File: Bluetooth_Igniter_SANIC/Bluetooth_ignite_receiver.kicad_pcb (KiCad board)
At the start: 2 copper layers, 62.3 x 30 mm, 68 parts, among them J1 Screw_Terminal_01x02, J2 Screw_Terminal_01x02, J3 Screw_Terminal_01x02, J4 Screw_Terminal_01x02, J5 USB_C_Receptacle_USB2.0, J6 Conn_01x02_Male, J7 Conn_01x02_Male, Q1 MMDT2222A, Q2 MMDT2222A, Q3 Q_NMOS_GSD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

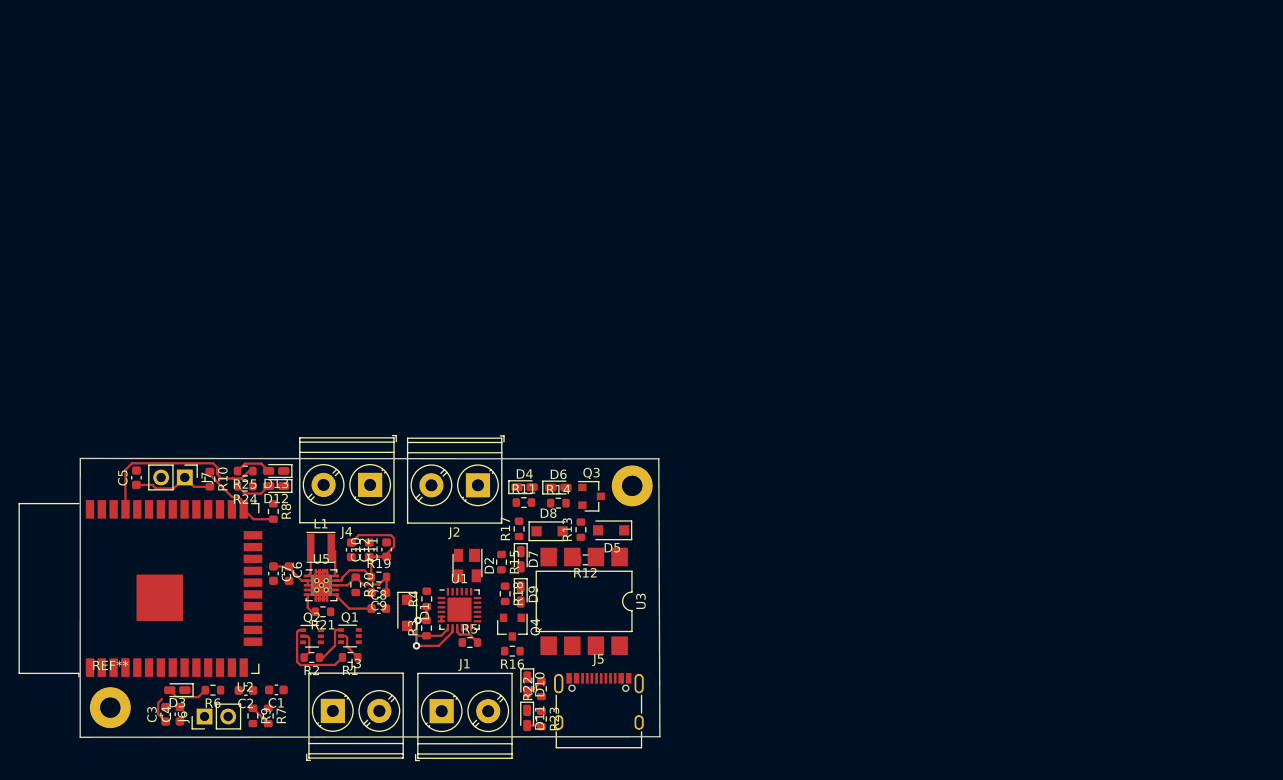
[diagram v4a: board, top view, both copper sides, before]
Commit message: need to fit pin headers in
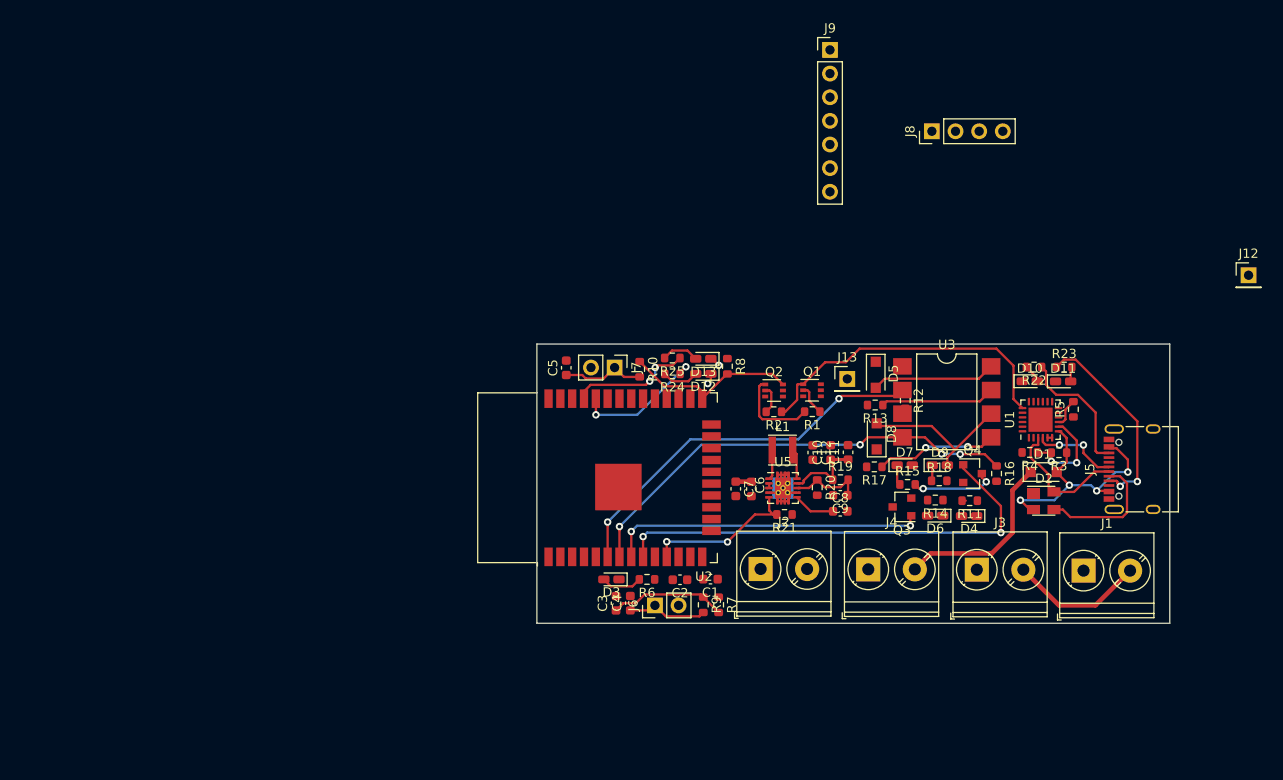
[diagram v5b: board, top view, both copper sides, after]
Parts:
- removed REF** (x2): MountingHole_2.2mm_M2_Pad, MountingHole:MountingHole_2.2mm_M2_Pad
- added J12: Conn_01x01_Male, Connector_PinHeader_2.54mm:PinHeader_1x01_P2.54mm_Vertical, F.Cu at (153.0, 67.9)
- added J13: Conn_01x01_Male, Connector_PinHeader_2.54mm:PinHeader_1x01_P2.54mm_Vertical, F.Cu at (109.9, 79.1)
- added J8: Conn_01x04_Male, Connector_PinHeader_2.54mm:PinHeader_1x04_P2.54mm_Vertical, F.Cu at (119.0, 52.5)
- added J9: Conn_01x07_Male, Connector_PinHeader_2.54mm:PinHeader_1x07_P2.54mm_Vertical, F.Cu at (108.1, 43.7)
- moved J3 70.8 mm to (123.9, 99.6)
- moved J1 70.6 mm to (135.3, 99.7)
- moved R3 70.5 mm to (132.7, 87.0), turned to 180 degrees
- moved D1 70.0 mm to (131.0, 89.1), turned to 0 degrees
- moved R5 69.5 mm to (134.2, 82.3), turned to 90 degrees
- moved D11 68.0 mm to (133.1, 79.3), turned to 0 degrees
- moved R23 67.7 mm to (133.2, 77.8), turned to 0 degrees
- moved R4 66.7 mm to (129.5, 87.0), turned to 180 degrees
- moved U1 65.7 mm to (130.7, 83.5), turned to 90 degrees
- moved J5 64.0 mm to (141.7, 88.8), turned to 90 degrees
- moved R22 63.2 mm to (130.0, 77.8), turned to 180 degrees
- moved D10 63.1 mm to (129.5, 79.3), turned to 0 degrees
- moved D2 62.3 mm to (131.0, 92.2), turned to 0 degrees
- moved Q1 56.2 mm to (106.1, 80.3)
- moved Q2 56.2 mm to (102.1, 80.3)
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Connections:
- U2 pad 29: Net-(U2-Pad29) -> /CS
- U2 pad 30: Net-(U2-Pad30) -> /CLK
- U2 pad 31: Net-(U2-Pad31) -> /MISO
- U2 pad 33: Net-(U2-Pad33) -> /SDA
- U2 pad 36: Net-(U2-Pad36) -> /SCL
- U2 pad 37: Net-(U2-Pad37) -> /MOSI
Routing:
- net /Nuke2: track 0.00 -> 49.8 mm, vias 0 -> 2
- net /Cont2: track 0.89 -> 49.9 mm, vias 0 -> 4
- net /Cont1: track 0.00 -> 41.3 mm, vias 0 -> 2
- net /Nuke1: track 0.00 -> 34.1 mm, vias 0 -> 2
- net /RTS: track 4.50 -> 34.4 mm
- net /usb/D-: track 0.00 -> 23.2 mm, vias 0 -> 2
- net /usb/VBUS: track 5.27 -> 27.6 mm, vias 0 -> 4
- net Net-(J5-PadA5): track 0.00 -> 21.8 mm, vias 0 -> 2
- net Net-(D8-Pad2): track 0.00 -> 17.1 mm
- net VDD: track 4.93 -> 21.8 mm
- net /PG: track 2.46 -> 17.1 mm, vias 0 -> 2
- net /pyros/Ext_supply: track 0.00 -> 14.6 mm
- net Net-(R24-Pad1): track 0.00 -> 14.6 mm, vias 0 -> 2
- net /usb/D+: track 0.00 -> 14.4 mm
- net Net-(J5-PadB5): track 0.00 -> 14.3 mm
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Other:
- board size 62.3 x 30 mm -> 68 x 30 mm

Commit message: Before copper fills
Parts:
- removed J12, J13: Conn_01x01_Male, Connector_PinHeader_2.54mm:PinHeader_1x01_P2.54mm_Vertical
- added J10: Conn_01x02_Male, Connector_PinHeader_2.54mm:PinHeader_1x02_P2.54mm_Vertical, F.Cu at (99.9, 98.8)
- added REF**: MountingHole_2.2mm_M2, MountingHole:MountingHole_2.2mm_M2, F.Cu at (146.3, 78.4)
- added REF**: MountingHole_2.2mm_M2, MountingHole:MountingHole_2.2mm_M2, F.Cu at (79.8, 102.4)
- moved J9 44.0 mm to (80.0, 77.7), turned to 90 degrees
- moved J8 31.6 mm to (107.2, 81.8)
- moved C5 19.2 mm to (99.0, 77.3)
- moved D12 19.2 mm to (113.7, 78.0)
- moved D13 19.2 mm to (113.7, 76.4)
- moved J7 19.2 mm to (104.2, 77.3)
- moved R10 19.2 mm to (106.9, 77.5)
- moved R25 19.2 mm to (110.4, 76.3)
- moved R8 19.2 mm to (116.3, 77.2)
- moved R24 19.2 mm to (110.4, 78.0)
- moved R11 12.1 mm to (112.9, 85.6), turned to 270 degrees
- moved D4 11.7 mm to (114.6, 85.7), turned to 270 degrees
- moved R14 7.11 mm to (112.8, 89.3), turned to 270 degrees
- moved D6 6.57 mm to (114.5, 89.4), turned to 270 degrees
- moved D7 5.87 mm to (121.6, 90.3)
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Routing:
- net /PG: track 17.1 -> 88.4 mm, vias 2 -> 3
- net /pyros/Ext_supply: track 14.6 -> 65.2 mm, vias 0 -> 5
- net /EN: track 12.5 -> 56.4 mm, vias 0 -> 4
- net Net-(D5-Pad2): track 13.4 -> 50.2 mm, vias 0 -> 2
- net /DTR: track 9.29 -> 44.7 mm, vias 0 -> 1
- net VDD: track 21.8 -> 54.2 mm, vias 0 -> 2
- net /TXD: track 1.18 -> 32.8 mm, vias 1 -> 2
- net /RXD: track 1.14 -> 29.1 mm, vias 1 -> 2
- net Net-(R25-Pad1): track 13.1 -> 37.6 mm, vias 2 -> 0
- net Net-(D5-Pad1): track 0.40 -> 18.8 mm
- net Net-(R24-Pad1): track 14.6 -> 32.2 mm
- net GND: track 11.4 -> 23.5 mm, vias 0 -> 2
- net /RTS: track 34.4 -> 46.0 mm, vias 0 -> 2
- net /BOOT: track 19.1 -> 30.4 mm, vias 0 -> 4
- net Net-(D8-Pad2): track 17.1 -> 27.3 mm
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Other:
- board size 68 x 30 mm -> 73 x 30 mm

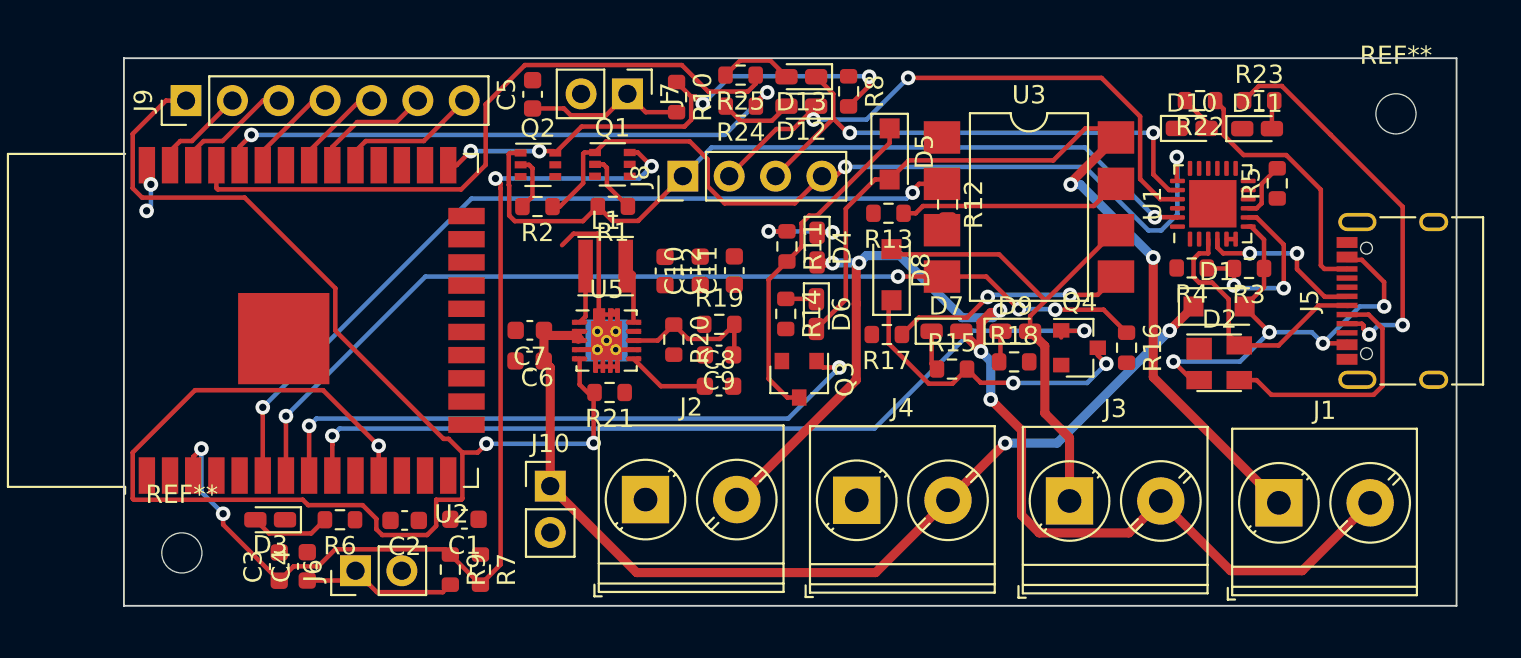
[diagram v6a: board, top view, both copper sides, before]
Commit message: After copper fill. Fully routed board
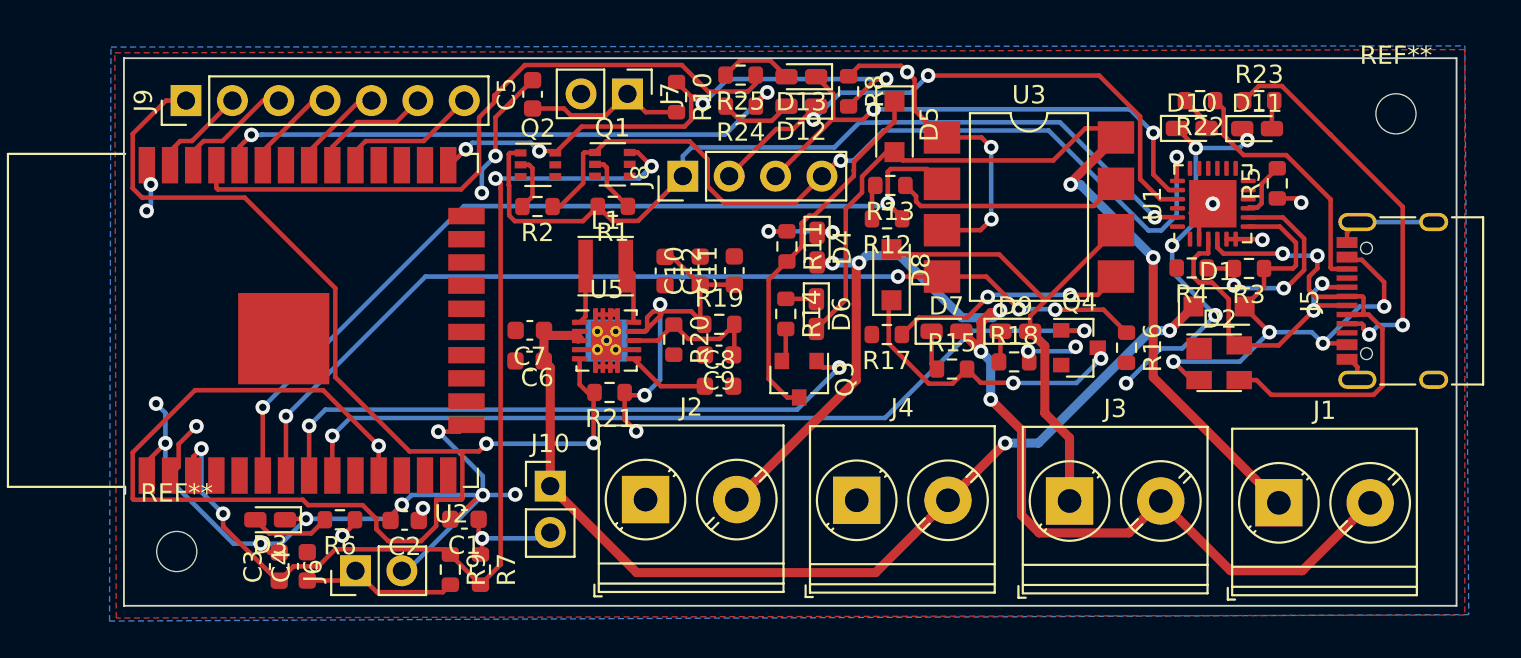
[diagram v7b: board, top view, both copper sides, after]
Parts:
- moved R12 3.41 mm to (118.4, 84.1), turned to 180 degrees
- moved R13 1.53 mm to (118.6, 82.3)
- moved D5 1.52 mm to (118.8, 79.1)
- moved REF** 0.29 mm to (79.5, 102.4)
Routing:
- net GND: track 23.5 -> 108.4 mm, vias 2 -> 20
- net +3V3: track 1.59 -> 56.5 mm, vias 0 -> 12
- net /usb/VBUS: track 27.6 -> 31.5 mm
- net /usb/D-: track 23.2 -> 26.9 mm
- net /usb/D+: track 14.7 -> 17.9 mm, vias 0 -> 2
- net /Cont1: track 46.1 -> 48.9 mm
- net Net-(R3-Pad2): track 10.2 -> 12.0 mm
- net /BOOT: track 30.4 -> 32.2 mm
- net /DTR: track 44.7 -> 46.5 mm
- net /PG: track 88.4 -> 90.2 mm
- net /RTS: track 46.0 -> 47.7 mm
- net Net-(D5-Pad1): track 18.8 -> 20.3 mm
- net Net-(D5-Pad2): track 50.2 -> 51.0 mm
- net Net-(D8-Pad1): track 17.4 -> 16.8 mm
- added copper zone on B.Cu, net +3V3
- added copper zone on F.Cu, net GND

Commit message: update
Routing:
- net /PG: track 90.2 -> 93.1 mm
- net +3V3: track 56.5 -> 58.1 mm
- net GND: track 108.4 -> 109.2 mm
